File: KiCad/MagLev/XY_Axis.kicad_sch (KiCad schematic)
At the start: 26 parts, among them Q1 2SD2673, Q2 2SB1708, Q3 2SD2673, Q4 2SB1708, U1 LM324

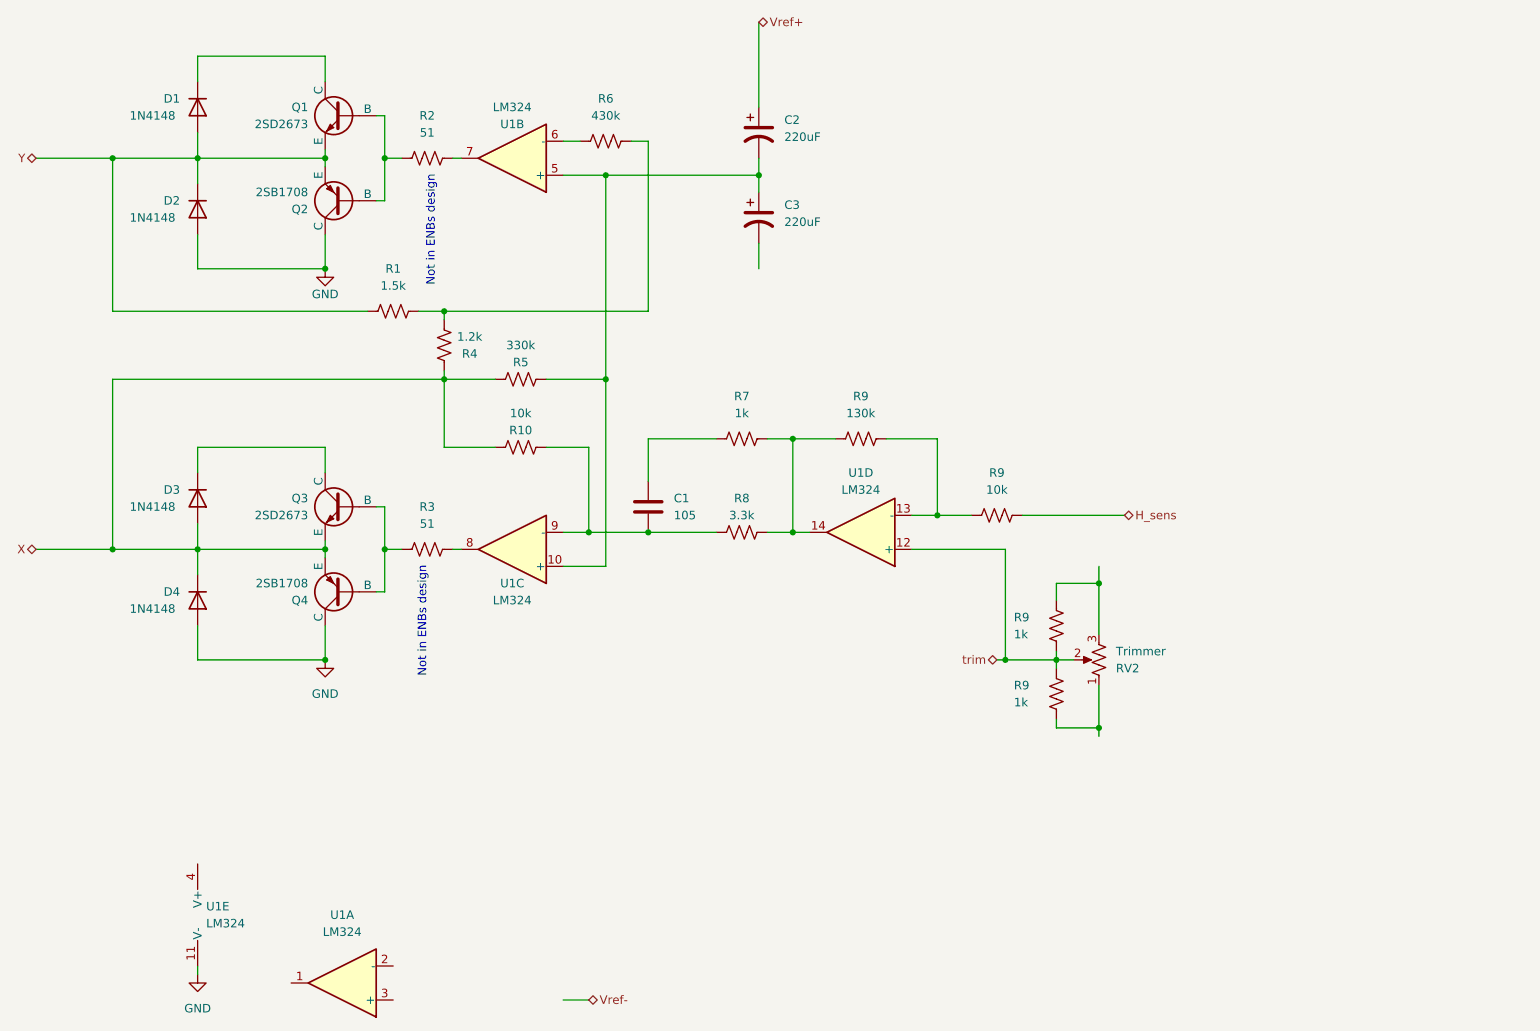
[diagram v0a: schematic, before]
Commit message: Complete schematic equivilant to ENBs.
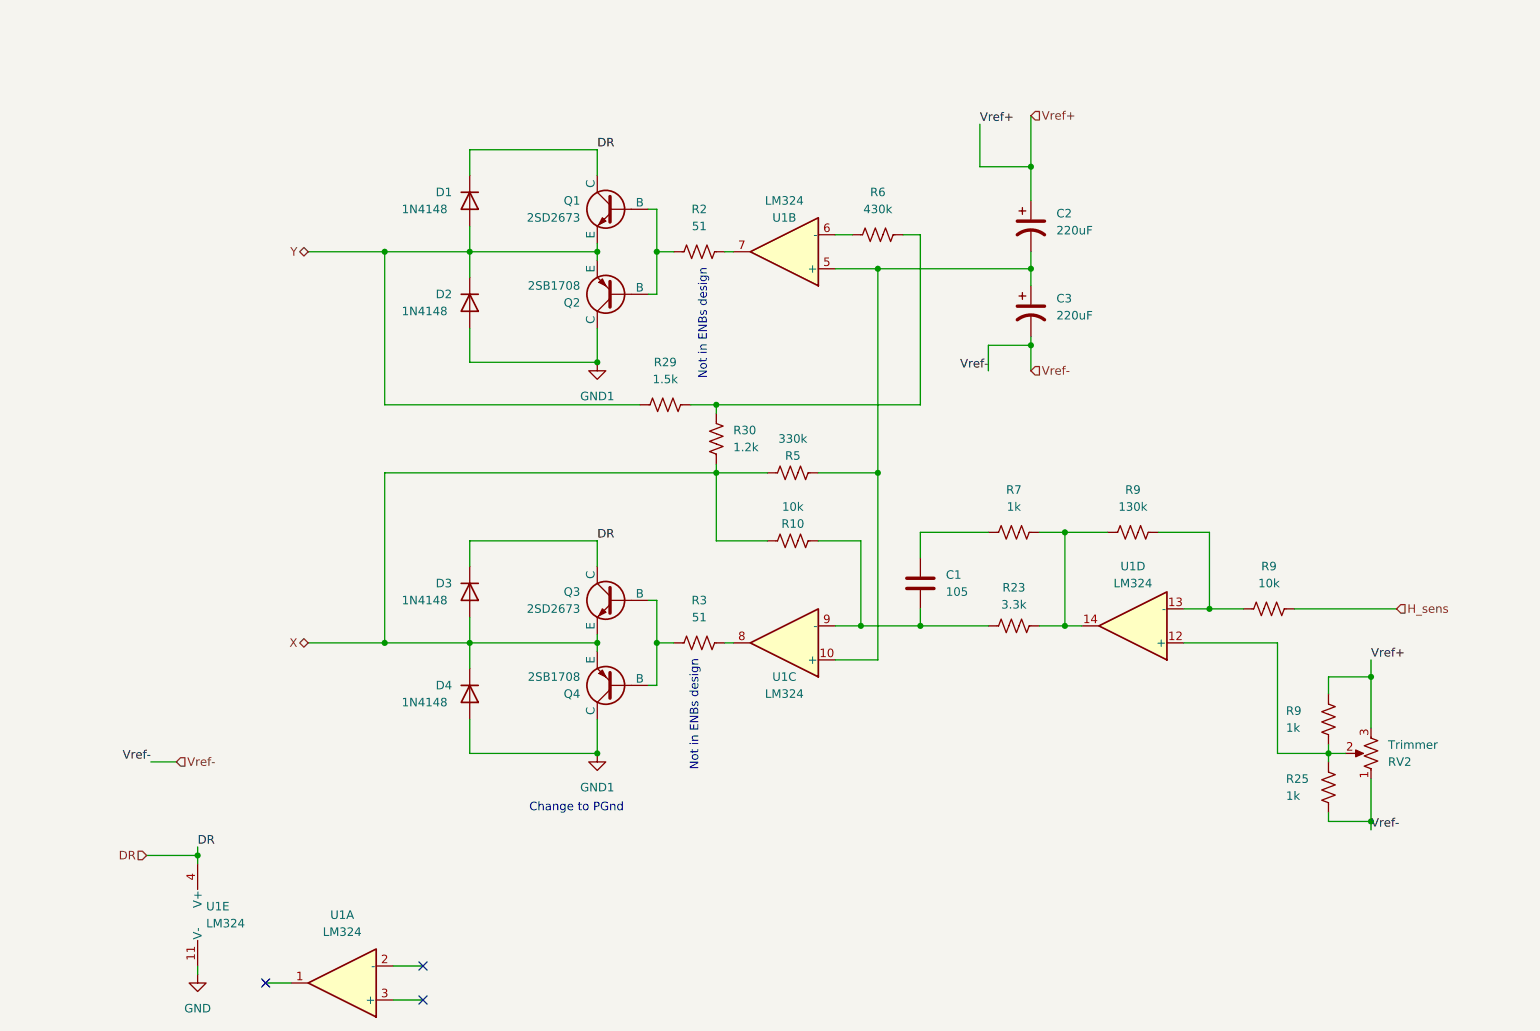
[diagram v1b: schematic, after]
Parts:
- removed R1: 1.5k, symbol Device:R_US
- removed R4: 1.2k, symbol Device:R_US
- removed R8: 3.3k, symbol Device:R_US
- removed R9: 1k, symbol Device:R_US
- added R23: 3.3k, symbol Device:R_US
- added R25: 1k, symbol Device:R_US
- added R29: 1.5k, symbol Device:R_US
- added R30: 1.2k, symbol Device:R_US
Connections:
- net GND: no longer D2.2 (A), D4.2 (A), Q2.1 (C), Q4.1 (C)
- net Vref+: now also R9.2, RV2.3
- net Vref-: now also C3.2, RV2.1, R25.2
- net X: now also R30.2
- net Y: now also R29.1
- net at R6.2: now also R29.2, R30.1
- net at C1.2, R10.1, U1.9 (-): now also R23.1
- net DR: now reaches U1.4 (V+)
- net DR: now also D1.1 (K), D3.1 (K), Q1.1 (C), Q3.1 (C)
- net at R7.2, R9.1, U1.14: now also R23.2
- net trim: no longer names the net of R9.1, RV2.2, U1.12 (+)
- net trim: now also R25.1
- new net GND1: D2.2 (A), D4.2 (A), Q2.1 (C), Q4.1 (C)
- no-connect marks 0 -> 3
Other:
- note added: "Change to PGnd"
- moved on the sheet: C1, C2, C3, D1, D2, D3, D4, Q1, Q2, Q3, Q4, R10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

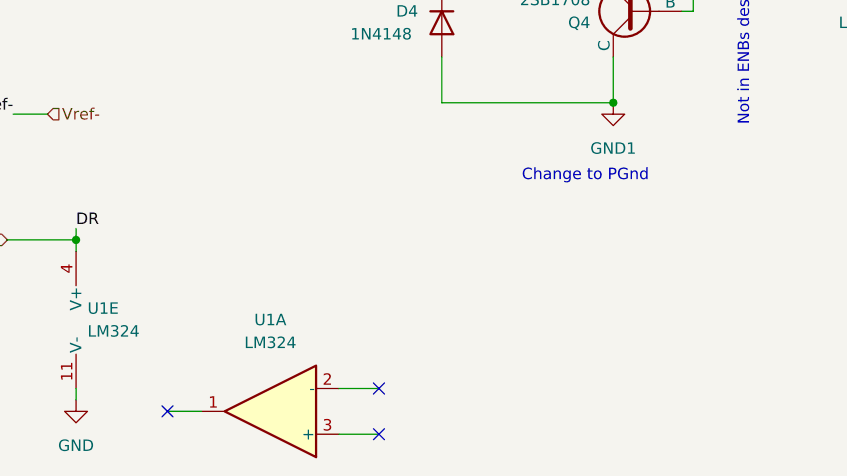
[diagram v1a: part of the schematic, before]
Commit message: Clean up schematics, add title block info.
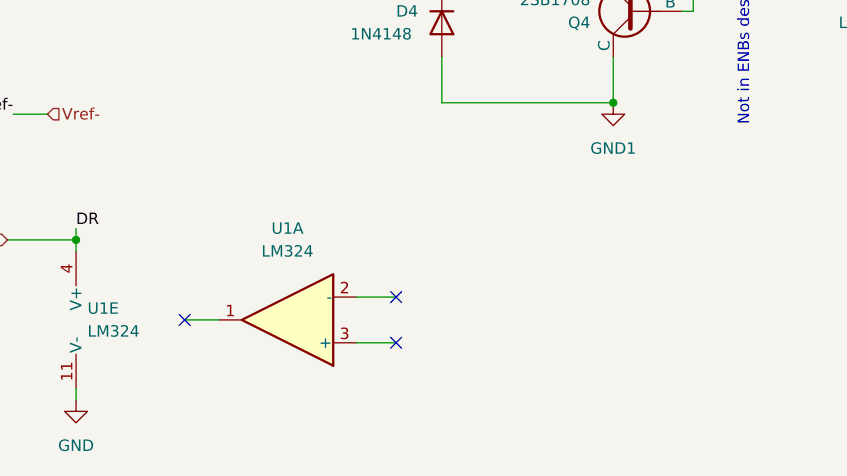
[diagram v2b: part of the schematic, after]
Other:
- note removed: "Change to PGnd"
- company: (none) -> Kevin Dueck
- title: (none) -> X-Y Axis Circuit
- moved on the sheet: U1A
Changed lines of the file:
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@@
 (kicad_sch (version 20230121) (generator eeschema)
   (paper "A4")
+  (title_block
+    (title "X-Y Axis Circuit")
+    (date "2023-08-06")
+    (rev "1.0")
+    (company "Kevin Dueck")
+  )
   (junction (at 45.72 151.13) (diameter 0) (color 0 0 0 0)
   )
@@
   (junction (at 123.19 93.98) (diameter 0) (color 0 0 0 0)
   )
-  (no_connect (at 55.88 170.18))
-  (no_connect (at 79.375 172.72))
-  (no_connect (at 79.375 167.64))
+  (no_connect (at 57.785 160.02))
+  (no_connect (at 81.28 162.56))
+  (no_connect (at 81.28 157.48))
   (wire (pts (xy 140.97 58.42) (xy 143.51 58.42))
     (stroke (width 0) (type default))
@@
     (stroke (width 0) (type default))
   )
-  (wire (pts (xy 74.93 172.72) (xy 79.375 172.72))
+  (wire (pts (xy 76.835 162.56) (xy 81.28 162.56))
     (stroke (width 0) (type default))
   )
@@
     (stroke (width 0) (type default))
   )
-  (wire (pts (xy 74.93 167.64) (xy 79.375 167.64))
-    (stroke (width 0) (type default))
-  )
-  (wire (pts (xy 55.88 170.18) (xy 59.69 170.18))
+  (wire (pts (xy 76.835 157.48) (xy 81.28 157.48))
+    (stroke (width 0) (type default))
+  )
+  (wire (pts (xy 57.785 160.02) (xy 61.595 160.02))
     (stroke (width 0) (type default))
   )
@@
   (wire (pts (xy 114.3 60.96) (xy 114.3 67.31))
     (stroke (width 0) (type default))
-  )
-  (text "Change to PGnd" (at 95.25 144.78 0)
-    (effects (font (size 1.27 1.27)) (justify left bottom))
   )
   (text "Not in ENBs design" (at 121.92 63.5 90)
@@
     )
   )
-  (symbol (lib_id "Amplifier_Operational:LM324") (at 67.31 170.18 180) (unit 1)
+  (symbol (lib_id "Amplifier_Operational:LM324") (at 69.215 160.02 180) (unit 1)
     (in_bom yes) (on_board yes) (dnp no) (fields_autoplaced)
-    (property "Reference" "U1" (at 67.31 160.02 0)
-      (effects (font (size 1.27 1.27)))
-    )
-    (property "Value" "LM324" (at 67.31 162.56 0)
-      (effects (font (size 1.27 1.27)))
-    )
-    (property "Footprint" "" (at 68.58 172.72 0)
-      (effects (font (size 1.27 1.27)) hide)
-    )
-    (property "Datasheet" "http://www.ti.com/lit/ds/symlink/lm2902-n.pdf" (at 66.04 175.26 0)
-      (effects (font (size 1.27 1.27)) hide)
-    )
+    (property "Reference" "U1" (at 69.215 149.86 0)
+      (effects (font (size 1.27 1.27)))
+    )
+    (property "Value" "LM324" (at 69.215 152.4 0)
+      (effects (font (size 1.27 1.27)))
+    )
+    (property "Footprint" "" (at 70.485 162.56 0)
+      (effects (font (size 1.27 1.27)) hide)
+    )
+    (property "Datasheet" "http://www.ti.com/lit/ds/symlink/lm2902-n.pdf" (at 67.945 165.1 0)
+      (effects (font (size 1.27 1.27)) hide)
+    )

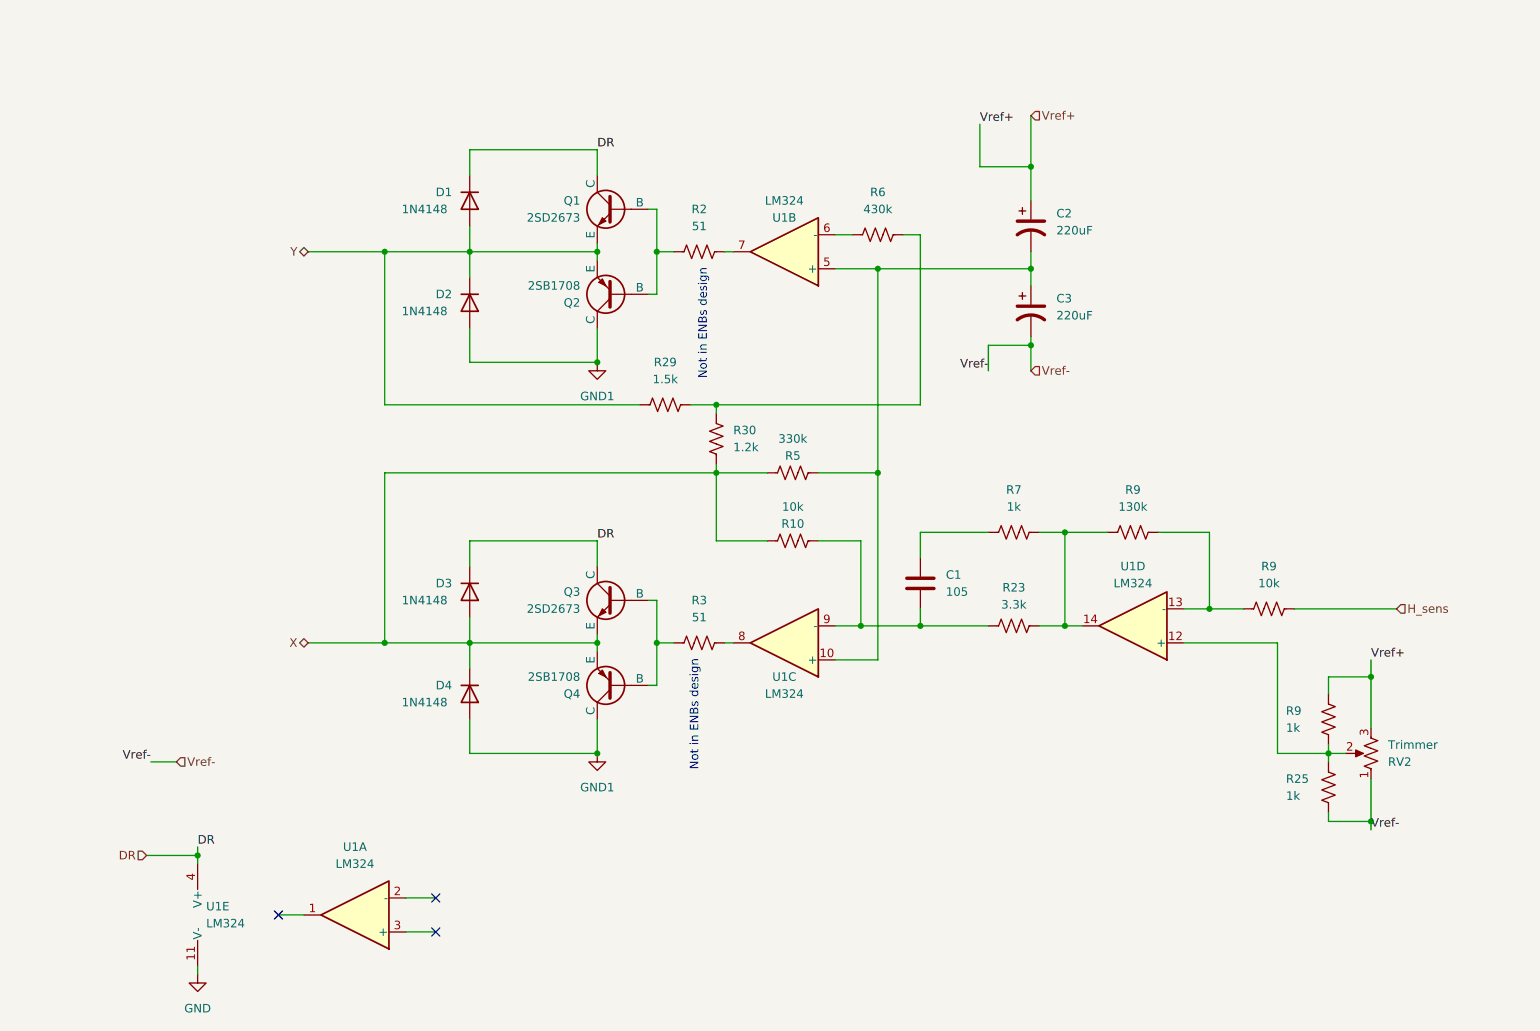
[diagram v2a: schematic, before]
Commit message: Add footprints to all components, add datasheet directory.
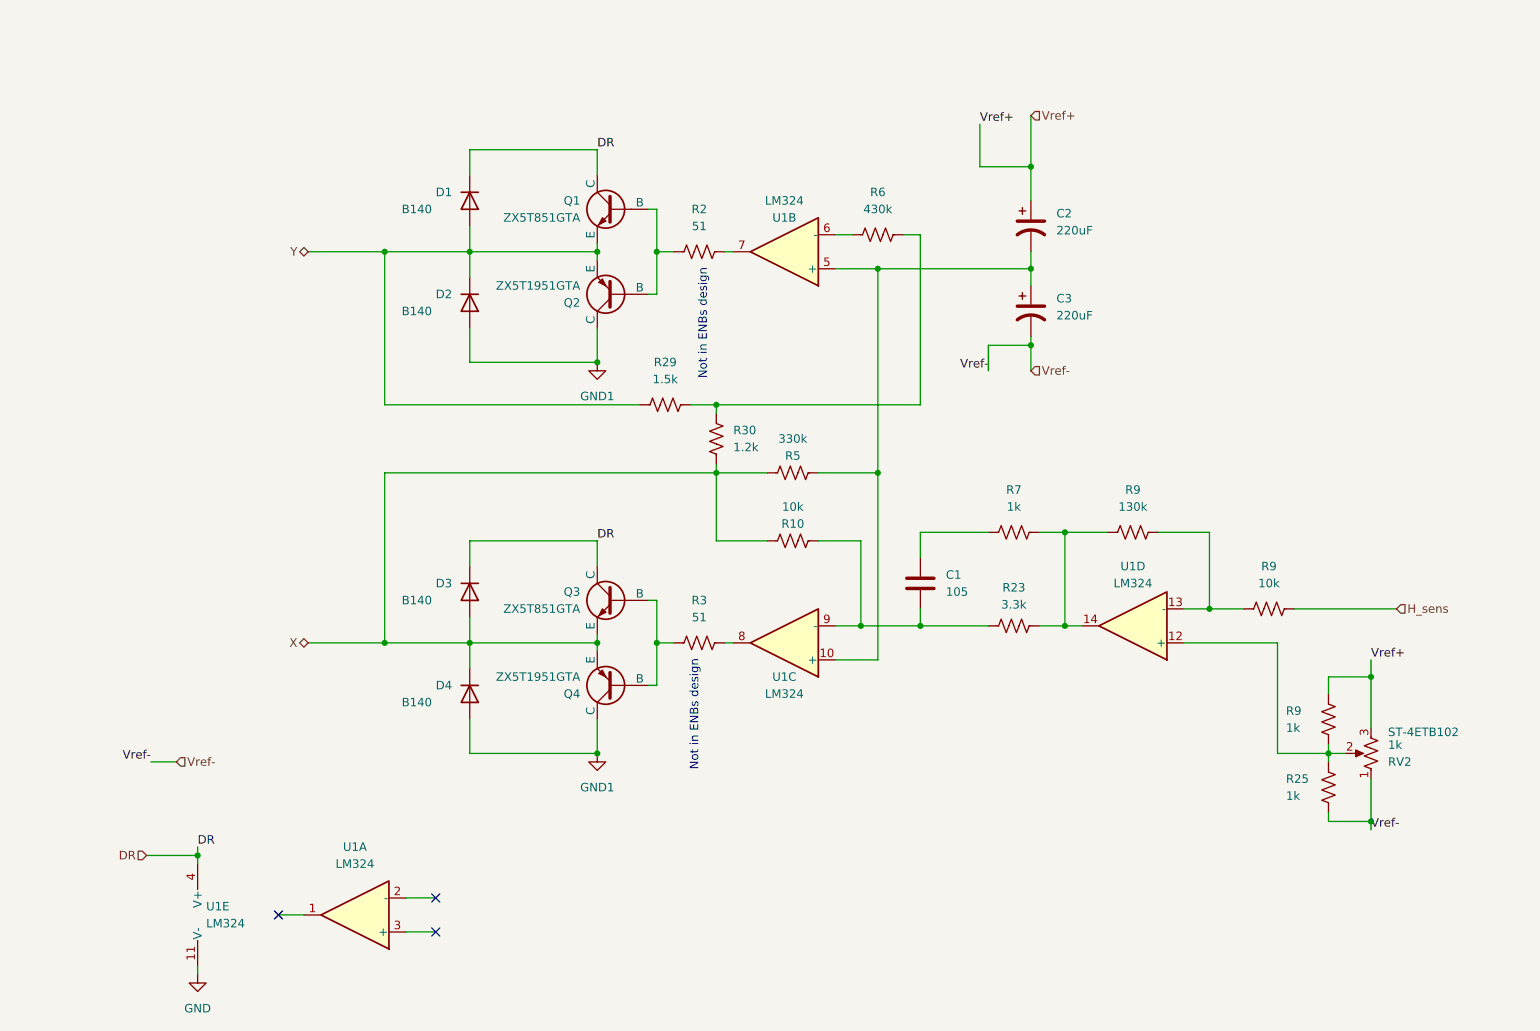
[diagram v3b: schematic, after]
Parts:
- C1: footprint (none) -> Capacitor_SMD:C_0805_2012Metric_Pad1.18x1.45mm_HandSolder
- C2, C3: footprint (none) -> Capacitor_SMD:CP_Elec_8x10
- D1, D2, D3, D4: value 1N4148 -> B140; footprint (none) -> Diode_SMD:D_SMA_Handsoldering
- Q1, Q3: value 2SD2673 -> ZX5T851GTA; footprint (none) -> Maglev_Footprint_Library:SOT-223-3_TabPin2_BJT
- Q2, Q4: value 2SB1708 -> ZX5T1951GTA; footprint (none) -> Maglev_Footprint_Library:SOT-223-3_TabPin2_BJT
- R10, R2, R23, R25, R29, R3, R30, R5, R6, R7, R9: footprint (none) -> Resistor_SMD:R_0805_2012Metric_Pad1.20x1.40mm_HandSolder
- RV2: value Trimmer -> 1k; footprint (none) -> Maglev_Footprint_Library:Potentiometer_ST-4EB; PN (none) -> ST-4ETB102
- U1: footprint (none) -> Package_SO:SOIC-14_3.9x8.7mm_P1.27mm
